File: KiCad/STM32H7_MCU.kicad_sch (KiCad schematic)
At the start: 52 parts, among them IC3 SN74LVC1G14DBVR, IC4 STM32H7R7L8H6H, IC5 TLV75718PDRVR, Y1 VXM7-9032-25M0000000

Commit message: #13
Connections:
- net DVID_SEL1 renamed VMUX_EN
- net DVID_SEL2 renamed VMUX_SEL
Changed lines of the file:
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@@
 	(title_block
 		(title "${project_name}")
-		(date "2026-01-17")
+		(date "2026-01-29")
 		(rev "${project_version}")
 		(company "${project_creator}")
@@
 	)
 	(no_connect
-		(at 71.12 43.18)
-	)
-	(no_connect
 		(at 71.12 134.62)
 	)
@@
 	)
 	(no_connect
+		(at 71.12 43.18)
+	)
+	(no_connect
 		(at 71.12 58.42)
 	)
@@
 		)
 	)
-	(global_label "DVID_SEL1"
+	(global_label "VMUX_EN"
 		(shape output)
 		(at 35.56 71.12 180)
@@
 		)
 		(property "Intersheetrefs" "${INTERSHEET_REFS}"
-			(at 27.0704 71.12 0)
+			(at 27.9595 71.12 0)
 			(effects
 				(font
@@
 		)
 	)
-	(global_label "DVID_SEL2"
+	(global_label "VMUX_SEL"
 		(shape output)
 		(at 76.2 147.32 0)
@@
 		)
 		(property "Intersheetrefs" "${INTERSHEET_REFS}"
-			(at 84.6896 147.32 0)
+			(at 84.4356 147.32 0)
 			(effects
 				(font

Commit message: #16
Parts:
- renumbered C11 to C10, C14 to C11, C18 to C12, C21 to C13, C26 to C14, C12 to C15, C24 to C16, C15 to C17, C8 to C18, C16 to C19, C19 to C20, C22 to C21, C27 to C22, C28 to C23, C23 to C24, C36 to C25, C39 to C26, C41 to C27, C29 to C28, C32 to C29, C34 to C30, C37 to C31, C30 to C32, C5 to C34, C38 to C36, C40 to C37, C42 to C38, C6 to C39, C9 to C4, C31 to C40, C4 to C41, C7 to C42, C10 to C5, C13 to C6, C17 to C7, C20 to C8, C25 to C9, IC4 to IC3, IC5 to IC4, IC3 to IC5, R4 to R1, R3 to R2, R1 to R3, R2 to R4

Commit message: #18, OSHW ID121
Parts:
- removed C41, C42: 1u, PCM_EEZ_passives:C_0402_1005Metric, symbol PCM_EEZ_passives:C-EU
- removed IC4: TLV75718PDRVR, PCM_EEZ_SMD:DRV0006A, symbol PCM_EEZ_TI:TLV75718PDRVR
- C10: renamed from C8; LCSC (none) -> C60474
- C11: renamed from C9; LCSC (none) -> C60474
- C12: renamed from C10; LCSC (none) -> C60474
- C13: renamed from C11; LCSC (none) -> C60474
- C14: renamed from C12; LCSC (none) -> C60474
- C15: renamed from C13; LCSC (none) -> C60474
- C16: renamed from C14; LCSC (none) -> C60474
- C20: renamed from C18; LCSC (none) -> C15195
- C25: renamed from C23; LCSC (none) -> C60474
- C27: renamed from C25; LCSC (none) -> C60474
- C28: renamed from C26; LCSC (none) -> C60474
- C31: renamed from C29; LCSC (none) -> C60474
- C32: renamed from C30; LCSC (none) -> C60474
- C33: renamed from C31; LCSC (none) -> C60474
- C35: renamed from C33; LCSC (none) -> C60474
- C36: renamed from C34; LCSC (none) -> C76945
- C37: renamed from C35; LCSC (none) -> C60474
- C38: renamed from C36; LCSC (none) -> C60474
- C39: renamed from C37; LCSC (none) -> C60474
- C41: renamed from C39; LCSC (none) -> C76945
- C42: renamed from C40; LCSC (none) -> C60474
- C7: renamed from C5; LCSC (none) -> C60474
- C8: renamed from C6; LCSC (none) -> C60474
- C9: renamed from C7; LCSC (none) -> C60474
- renumbered C15 to C17, C16 to C18, C17 to C19, C19 to C21, C20 to C22, C21 to C23, C22 to C24, C24 to C26, C27 to C29, C28 to C30, C32 to C34, C38 to C40, C4 to C6, IC3 to IC4
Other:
- note removed: "+1V8 LDO (max 1A)"

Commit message: #19
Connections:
- net ~{SD_DETECT}: now reaches IC4.D10 (PM0)
- net SDMMC_D4: no longer names the net of IC4.B1 (PB8)
- net SDMMC_D5: no longer names the net of IC4.C2 (PB9)
- net SDMMC_D6: no longer names the net of IC4.E15 (PC6)
- net SDMMC_D7: no longer names the net of IC4.F13 (PC7)
- no-connect marks 23 -> 26
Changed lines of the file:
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@@
 	(title_block
 		(title "${project_name}")
-		(date "2026-04-04")
+		(date "2026-04-09")
 		(rev "${project_version}")
 		(company "${project_creator}")
@@
 	)
 	(no_connect
-		(at 149.86 27.94)
-	)
-	(no_connect
 		(at 119.38 68.58)
 	)
@@
 	)
 	(no_connect
+		(at 40.64 129.54)
+	)
+	(no_connect
 		(at 71.12 38.1)
 	)
@@
 	)
 	(no_connect
+		(at 40.64 132.08)
+	)
+	(no_connect
 		(at 71.12 134.62)
 	)
@@
 	)
 	(no_connect
+		(at 40.64 93.98)
+	)
+	(no_connect
 		(at 81.28 187.96)
 	)
@@
 	)
 	(no_connect
+		(at 40.64 91.44)
+	)
+	(no_connect
 		(at 71.12 43.18)
 	)
@@
 	)
 	(bus_entry
-		(at 17.78 91.44)
-		(size 2.54 2.54)
-		(stroke
-			(width 0)
-			(type default)
-		)
-	)
-	(bus_entry
 		(at 106.68 91.44)
 		(size -2.54 2.54)
@@
 	)
 	(bus_entry
-		(at 17.78 129.54)
-		(size 2.54 2.54)
-		(stroke
-			(width 0)
-			(type default)
-		)
-	)
-	(bus_entry
 		(at 106.68 93.98)
 		(size -2.54 2.54)
@@
 	)
 	(bus_entry
-		(at 17.78 127)
-		(size 2.54 2.54)
-		(stroke
-			(width 0)
-			(type default)
-		)
-	)
-	(bus_entry
 		(at 17.78 139.7)
 		(size 2.54 2.54)
@@
 	)
 	(bus_entry
-		(at 17.78 88.9)
-		(size 2.54 2.54)
-		(stroke
-			(width 0)
-			(type default)
-		)
-	)
-	(bus_entry
 		(at 106.68 104.14)
 		(size -2.54 2.54)
@@
 	(bus
 		(pts
-			(xy 17.78 86.36) (xy 17.78 88.9)
+			(xy 17.78 129.54) (xy 17.78 132.08)
 		)
 		(stroke
@@
 	(wire
 		(pts
-			(xy 20.32 91.44) (xy 40.64 91.44)
-		)
-		(stroke
-			(width 0)
-			(type default)
-		)
-	)
-	(wire
-		(pts
 			(xy 254 119.38) (xy 259.08 119.38)
 		)
@@
 	(wire
 		(pts
-			(xy 20.32 132.08) (xy 40.64 132.08)
-		)
-		(stroke
-			(width 0)
-			(type default)
-		)
-	)
-	(wire
-		(pts
 			(xy 170.18 55.88) (xy 175.26 55.88)
 		)
@@
 		)
 	)
-	(bus
-		(pts
-			(xy 17.78 127) (xy 17.78 129.54)
-		)
-		(stroke
-			(width 0)
-			(type default)
-			(color 0 72 72 1)
-		)
-	)
 	(wire
 		(pts
@@
 	(wire
 		(pts
+			(xy 154.94 27.94) (xy 149.86 27.94)
+		)
+		(stroke
+			(width 0)
+			(type default)
+		)
+	)
+	(wire
+		(pts
 			(xy 198.12 27.94) (xy 203.2 27.94)
 		)
@@
 		)
 	)
-	(bus
-		(pts
-			(xy 17.78 88.9) (xy 17.78 91.44)
-		)
-		(stroke
-			(width 0)
-			(type default)
-			(color 0 72 72 1)
-		)
-	)
 	(wire
 		(pts
@@
 	(wire
 		(pts
-			(xy 20.32 93.98) (xy 40.64 93.98)
-		)
-		(stroke
-			(width 0)
-			(type default)
-		)
-	)
-	(wire
-		(pts
 			(xy 106.68 101.6) (xy 119.38 101.6)
 		)
@@
 		)
 	)
-	(bus
-		(pts
-			(xy 17.78 129.54) (xy 17.78 132.08)
-		)
-		(stroke
-			(width 0)
-			(type default)
-			(color 0 72 72 1)
-		)
-	)
 	(wire
 		(pts
@@
 		)
 	)
+	(bus
+		(pts
+			(xy 17.78 132.08) (xy 17.78 134.62)
+		)
+		(stroke
+			(width 0)
+			(type default)
+			(color 0 72 72 1)
+		)
+	)
 	(wire
 		(pts
@@
 		)
 	)
-	(bus
-		(pts
-			(xy 17.78 91.44) (xy 17.78 127)
-		)
-		(stroke
-			(width 0)
-			(type default)
-			(color 0 72 72 1)
-		)
-	)
 	(wire
 		(pts
@@
 	(wire
 		(pts
-			(xy 20.32 129.54) (xy 40.64 129.54)
-		)
-		(stroke
-			(width 0)
-			(type default)
-		)
-	)
-	(wire
-		(pts
 			(xy 106.68 99.06) (xy 119.38 99.06)
 		)
@@
 		)
 	)
-	(bus
-		(pts
-			(xy 17.78 132.08) (xy 17.78 134.62)
-		)
-		(stroke
-			(width 0)
-			(type default)
-			(color 0 72 72 1)
-		)
-	)
 	(wire
 		(pts
@@
 		)
 	)
-	(label "SDMMC_D5"
-		(at 22.86 93.98 0)
-		(effects
-			(font
-				(size 0.889 0.889)
-			)
-			(justify left bottom)
-		)
-	)
 	(label "XSPIM_P1_IO14"
 		(at 109.22 109.22 0)
@@
 		)
 	)
-	(label "SDMMC_D7"
-		(at 22.86 132.08 0)
-		(effects
-			(font
-				(size 0.889 0.889)
-			)
-			(justify left bottom)
-		)
-	)
 	(label "XSPIM_P1_IO7"
 		(at 109.22 91.44 0)
@@
 		)
 	)
-	(label "SDMMC_D6"
-		(at 22.86 129.54 0)
-		(effects
-			(font
-				(size 0.889 0.889)
-			)
-			(justify left bottom)
-		)
-	)
 	(label "RCC_OSC_IN"
 		(at 83.82 63.5 180)
@@
 		)
 	)
-	(label "SDMMC_D4"
-		(at 22.86 91.44 0)
-		(effects
-			(font
-				(size 0.889 0.889)
-			)
-			(justify left bottom)
-		)
-	)
 	(label "XSPIM_P1_IO10"
 		(at 109.22 99.06 0)
@@
 		)
 	)
-	(global_label "SDMMC_CMD"
-		(shape bidirectional)
-		(at 76.2 33.02 0)
-		(fields_autoplaced yes)
-		(effects
-			(font
-				(size 0.889 0.889)
-				(color 132 132 0 1)
-			)
-			(justify left)
-		)
-		(property "Intersheetrefs" "${INTERSHEET_REFS}"
-			(at 86.6264 33.02 0)
-			(effects
-				(font
-					(size 1.27 1.27)
-				)
-				(justify left)
-				(hide yes)
-			)
-		)
-	)
 	(global_label "MCU_USB_UP_TX+"
 		(shape bidirectional)
@@
 		)
 	)
+	(global_label "SDMMC_CMD"
+		(shape bidirectional)
+		(at 76.2 33.02 0)
+		(fields_autoplaced yes)
+		(effects
+			(font
+				(size 0.889 0.889)
+				(color 0 72 72 1)
+			)
+			(justify left)
+		)
+		(property "Intersheetrefs" "${INTERSHEET_REFS}"
+			(at 86.6264 33.02 0)
+			(effects
+				(font
+					(size 1.27 1.27)
+				)
+				(justify left)
+				(hide yes)
+			)
+		)
+	)
 	(global_label "RS485_RX{slash}DIN3"
 		(shape input)
@@
 		)
 	)
+	(global_label "SDMMC_CLK"
+		(shape output)
+		(at 35.56 144.78 180)
+		(fields_autoplaced yes)
+		(effects
+			(font
+				(size 0.889 0.889)
+				(color 0 72 72 1)
+			)
+			(justify right)
+		)
+		(property "Intersheetrefs" "${INTERSHEET_REFS}"
+			(at 26.0967 144.78 0)
+			(effects
+				(font
+					(size 1.27 1.27)
+				)
+				(justify right)
+				(hide yes)
+			)
+		)
+	)
 	(global_label "VMUX_SEL"
 		(shape output)
@@
 		)
 	)
+	(global_label "~{SD_DETECT}"
+		(shape input)
+		(at 154.94 27.94 0)
+		(fields_autoplaced yes)
+		(effects
+			(font
+				(size 0.889 0.889)
+			)
+			(justify left)
+		)
+		(property "Intersheetrefs" "${INTERSHEET_REFS}"
+			(at 163.7258 27.94 0)
+			(effects
+				(font
+					(size 1.27 1.27)
+				)
+				(justify left)
+				(hide yes)
+			)
+		)
+	)
 	(global_label "~{DIB5_IRQ}"
 		(shape input)
@@
 	(global_label "{SDMMC_D[0..7]}"
 		(shape bidirectional)
-		(at 17.78 86.36 90)
+		(at 17.78 129.54 90)
 		(fields_autoplaced yes)
 		(effects
@@
 		)
 		(property "Intersheetrefs" "${INTERSHEET_REFS}"
-			(at 17.78 72.9278 90)
+			(at 17.78 116.1078 90)
 			(effects
 				(font
@@
 				(hide yes)
 			)
-		)
-	)
-	(global_label "SDMMC_CLK"
-		(shape output)
-		(at 35.56 144.78 180)
-		(fields_autoplaced yes)
-		(effects
-			(font
-				(size 0.889 0.889)
-				(color 132 132 0 1)
-			)
-			(justify right)
-		)
-		(property "Intersheetrefs" "${INTERSHEET_REFS}"
-			(at 26.0967 144.78 0)
-			(effects
-				(font
-					(size 1.27 1.27)
-				)
-				(justify right)
-				(hide yes)
-			)

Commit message: .step file update, migration to KiCad 10
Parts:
- X1: value ~ -> (none)

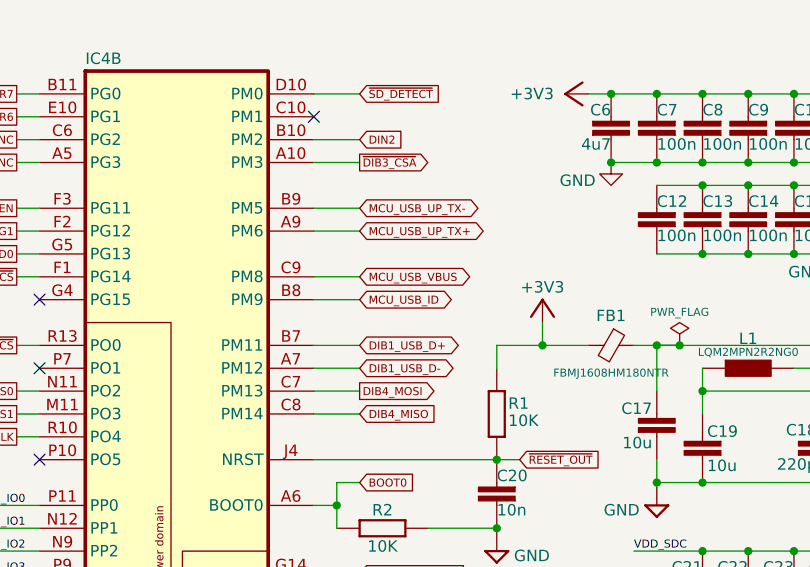
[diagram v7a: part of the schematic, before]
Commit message: USB lanes renamed, OSHWA logo added
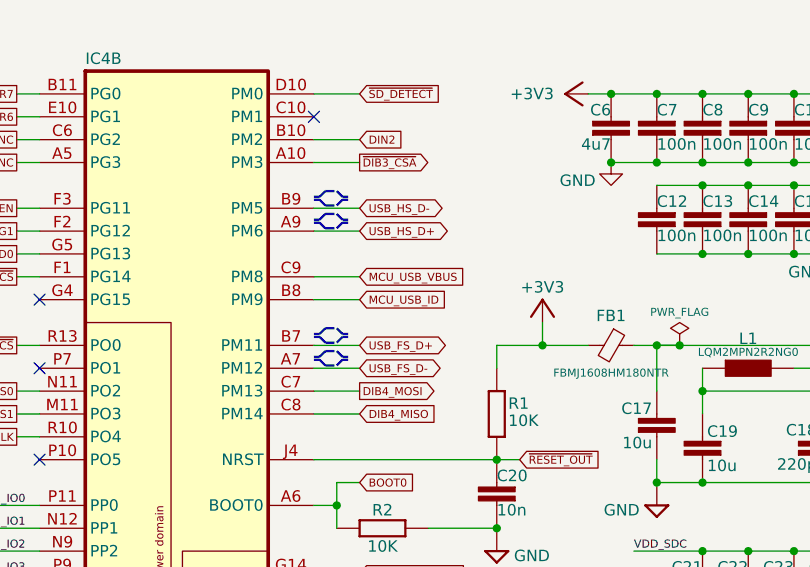
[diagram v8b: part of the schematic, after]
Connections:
- net DIB1_USB_D+ renamed USB_FS_D+
- net DIB1_USB_D- renamed USB_FS_D-
- net MCU_USB_UP_TX+ renamed USB_HS_D+
- net MCU_USB_UP_TX- renamed USB_HS_D-
